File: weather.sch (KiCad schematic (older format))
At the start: 24 parts, among them J1 Tag-Connect, U1 nRF52810-QCxx, U2 HDC2080, Y1 32MHz, Y2 32kHz

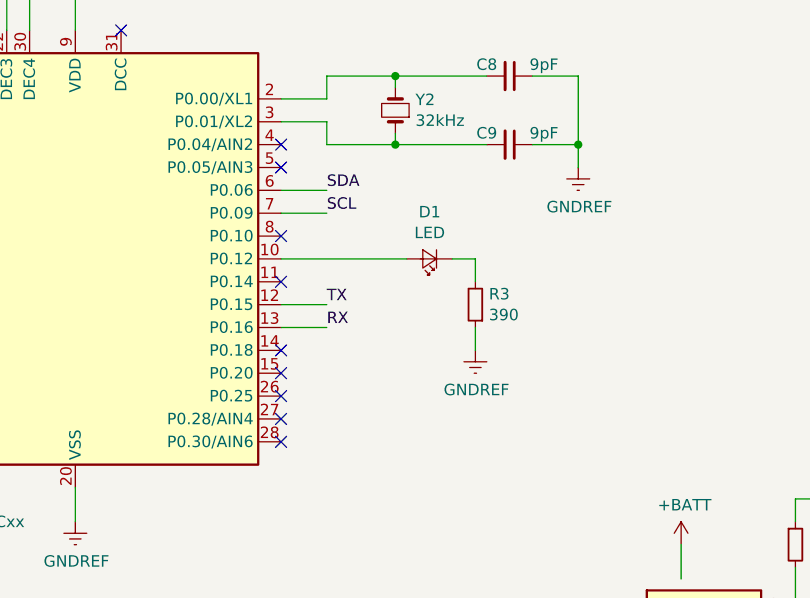
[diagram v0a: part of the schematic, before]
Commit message: Move LED to analog pin
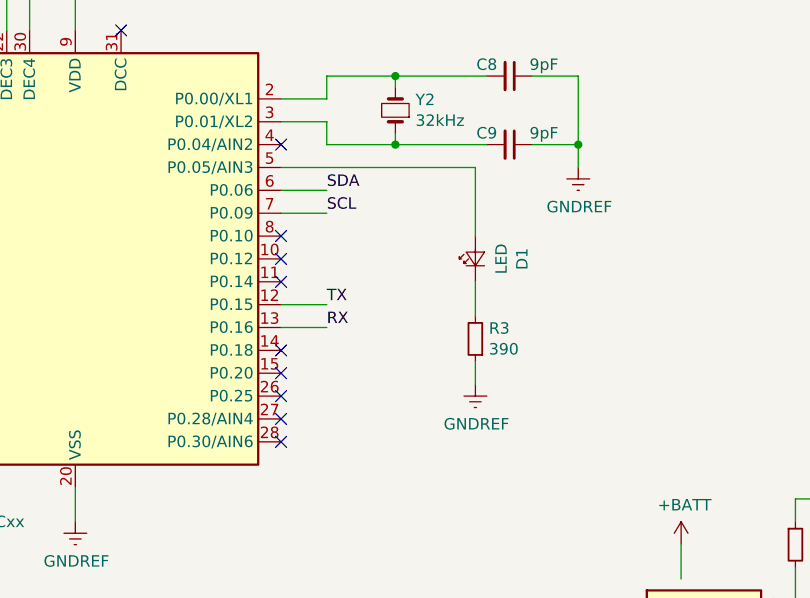
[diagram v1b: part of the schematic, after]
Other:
- moved on the sheet: D1, R3
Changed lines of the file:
@@
 NoConn ~ 4050 4250
 NoConn ~ 4050 3950
-NoConn ~ 4050 3450
+NoConn ~ 4050 3850
 NoConn ~ 4050 3350
 $Comp
@@
 L Device:LED_Small D1
 U 1 1 5B965F3F
-P 4700 3850
-F 0 "D1" H 4700 3645 50  0000 C CNN
-F 1 "LED" H 4700 3736 50  0000 C CNN
-F 2 "LED_SMD:LED_0603_1608Metric" V 4700 3850 50  0001 C CNN
-F 3 "~" V 4700 3850 50  0001 C CNN
-	1    4700 3850
-	-1   0    0    1
+P 4900 3850
+F 0 "D1" H 4900 3645 50  0000 C CNN
+F 1 "LED" H 4900 3736 50  0000 C CNN
+F 2 "LED_SMD:LED_0603_1608Metric" V 4900 3850 50  0001 C CNN
+F 3 "~" V 4900 3850 50  0001 C CNN
+	1    4900 3850
+	0    -1   -1   0
 $EndComp
 $Comp
 L Device:R_Small R3
 U 1 1 5B966096
-P 4900 4050
-F 0 "R3" H 4841 4004 50  0000 R CNN
-F 1 "390" H 4841 4095 50  0000 R CNN
-F 2 "Resistor_SMD:R_0603_1608Metric" H 4900 4050 50  0001 C CNN
-F 3 "~" H 4900 4050 50  0001 C CNN
-	1    4900 4050
+P 4900 4200
+F 0 "R3" H 4841 4154 50  0000 R CNN
+F 1 "390" H 4841 4245 50  0000 R CNN
+F 2 "Resistor_SMD:R_0603_1608Metric" H 4900 4200 50  0001 C CNN
+F 3 "~" H 4900 4200 50  0001 C CNN
+	1    4900 4200
 	-1   0    0    1
 $EndComp
@@
 L power:GNDREF #PWR0112
 U 1 1 5B9661A7
-P 4900 4250
-F 0 "#PWR0112" H 4900 4000 50  0001 C CNN
-F 1 "GNDREF" H 4905 4077 50  0000 C CNN
-F 2 "" H 4900 4250 50  0001 C CNN
-F 3 "" H 4900 4250 50  0001 C CNN
-	1    4900 4250
-	1    0    0    -1
-$EndComp
-Wire Wire Line
-	4900 4150 4900 4250
-Wire Wire Line
-	4900 3950 4900 3850
-Wire Wire Line
-	4900 3850 4800 3850
-Wire Wire Line
-	4600 3850 4050 3850
+P 4900 4400
+F 0 "#PWR0112" H 4900 4150 50  0001 C CNN
+F 1 "GNDREF" H 4905 4227 50  0000 C CNN
+F 2 "" H 4900 4400 50  0001 C CNN
+F 3 "" H 4900 4400 50  0001 C CNN
+	1    4900 4400
+	1    0    0    -1
+$EndComp
+Wire Wire Line
+	4900 4300 4900 4400
 NoConn ~ 4050 3750
 $Comp
@@
 Wire Wire Line
 	8400 4600 8400 4500
+Wire Wire Line
+	4900 3450 4900 3750
+Wire Wire Line
+	4050 3450 4900 3450
+Wire Wire Line
+	4900 3950 4900 4100
 $EndSCHEMATC

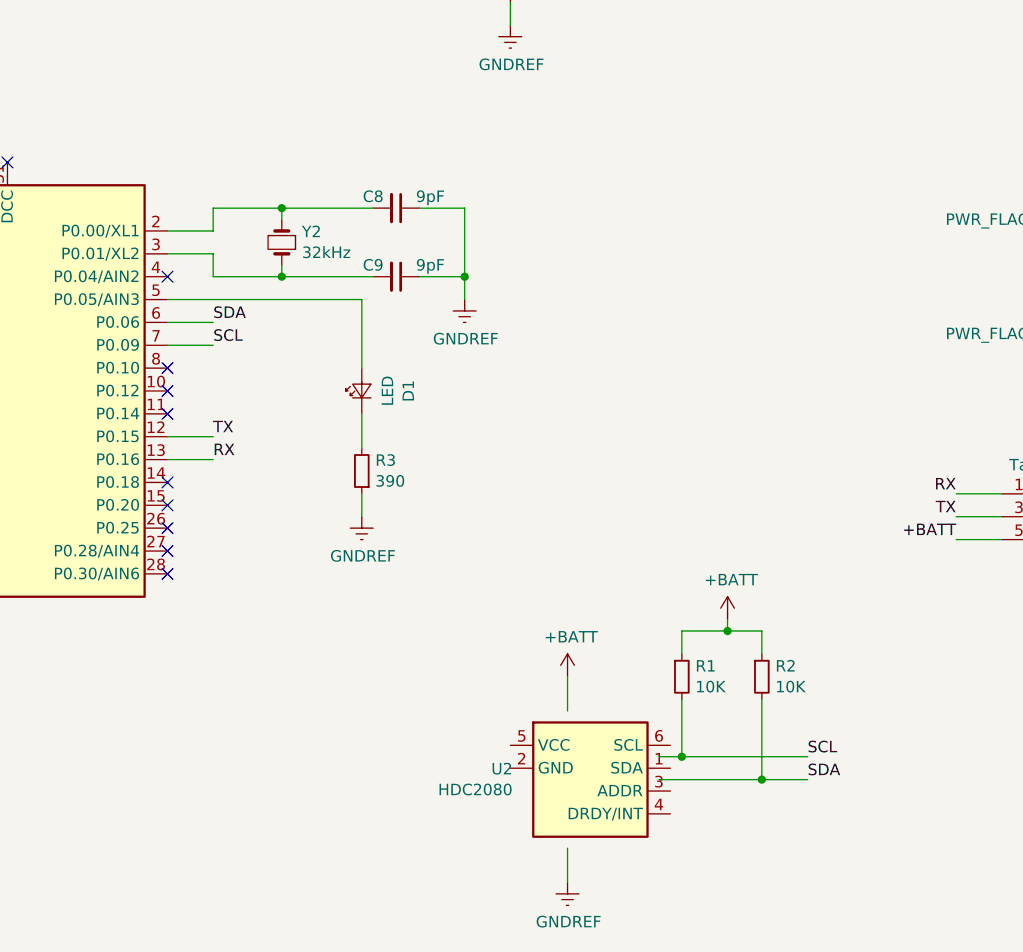
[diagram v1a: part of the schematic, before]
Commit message: HDC2080 DRDY / INT pin, and move LED pin
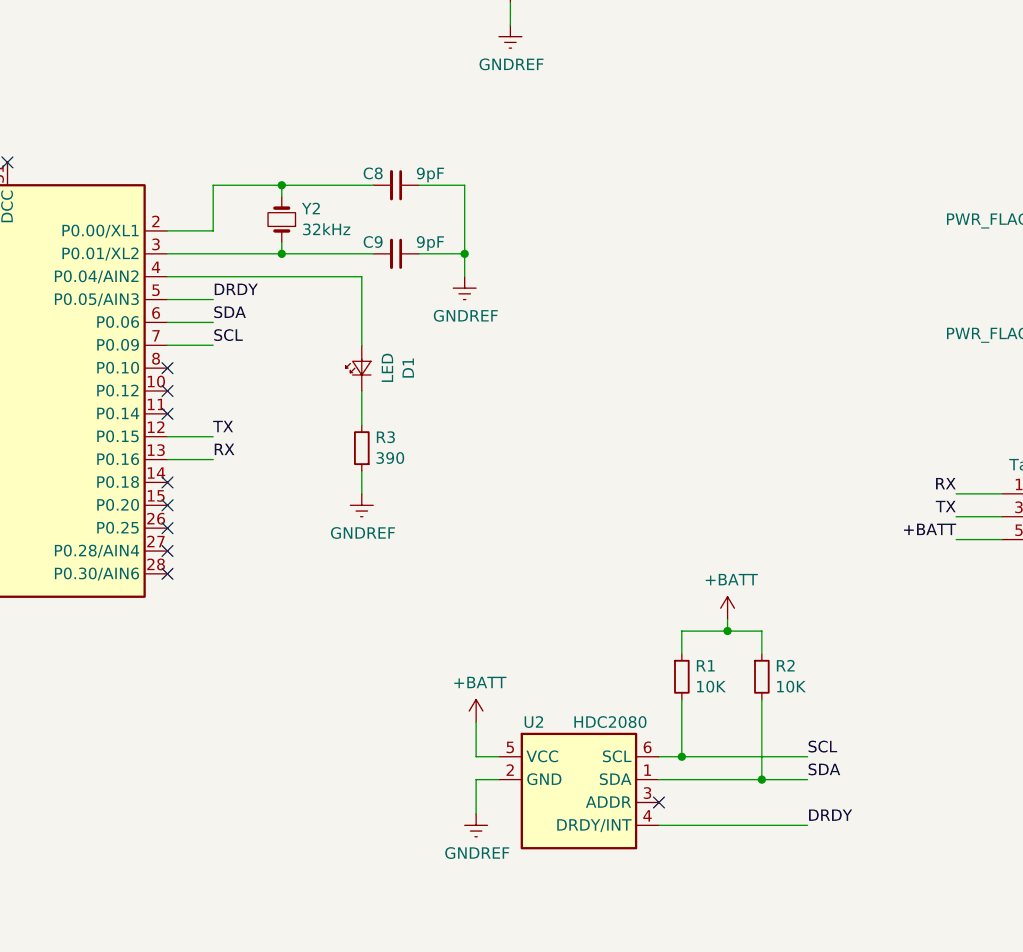
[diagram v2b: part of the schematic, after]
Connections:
- net labels added: DRDY
- wire segments 98 -> 100
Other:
- moved on the sheet: C8, C9, D1, R3, U2, Y2
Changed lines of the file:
@@
 L power:GNDREF #PWR0104
 U 1 1 5B7F3B6B
-P 5800 6000
-F 0 "#PWR0104" H 5800 5750 50  0001 C CNN
-F 1 "GNDREF" H 5805 5827 50  0000 C CNN
-F 2 "" H 5800 6000 50  0001 C CNN
-F 3 "" H 5800 6000 50  0001 C CNN
-	1    5800 6000
-	1    0    0    -1
-$EndComp
-Wire Wire Line
-	5800 5850 5800 6000
+P 5400 5700
+F 0 "#PWR0104" H 5400 5450 50  0001 C CNN
+F 1 "GNDREF" H 5405 5527 50  0000 C CNN
+F 2 "" H 5400 5700 50  0001 C CNN
+F 3 "" H 5400 5700 50  0001 C CNN
+	1    5400 5700
+	1    0    0    -1
+$EndComp
+Wire Wire Line
+	5400 5550 5400 5700
 $Comp
 L power:GNDREF #PWR0105
@@
 L power:+BATT #PWR0107
 U 1 1 5B7FB9F7
-P 5800 5100
-F 0 "#PWR0107" H 5800 4950 50  0001 C CNN
-F 1 "+BATT" H 5815 5273 50  0000 C CNN
-F 2 "" H 5800 5100 50  0001 C CNN
-F 3 "" H 5800 5100 50  0001 C CNN
-	1    5800 5100
+P 5400 5300
+F 0 "#PWR0107" H 5400 5150 50  0001 C CNN
+F 1 "+BATT" H 5415 5473 50  0000 C CNN
+F 2 "" H 5400 5300 50  0001 C CNN
+F 3 "" H 5400 5300 50  0001 C CNN
+	1    5400 5300
 	1    0    0    -1
 $EndComp
@@
 Connection ~ 3150 1800
 Wire Wire Line
-	5800 5100 5800 5250
+	5400 5300 5400 5450
 NoConn ~ 4050 4650
 NoConn ~ 4050 4550
@@
 NoConn ~ 4050 3950
 NoConn ~ 4050 3850
-NoConn ~ 4050 3350
 $Comp
 L Device:Battery_Cell BT1
@@
 L Anders_ICs:HDC2080 U2
 U 1 1 5B8027FD
-P 5900 5550
-F 0 "U2" H 5560 5596 50  0000 R CNN
-F 1 "HDC2080" H 5560 5505 50  0000 R CNN
-F 2 "Package_SON:Texas_PWSON-N6" H 5850 5300 50  0001 L CNN
-F 3 "http://www.ti.com/lit/ds/symlink/hdc2080.pdf" H 5500 5800 50  0001 C CNN
-	1    5900 5550
+P 5850 5600
+F 0 "U2" H 5700 5900 50  0000 R CNN
+F 1 "HDC2080" H 6150 5900 50  0000 R CNN
+F 2 "Package_SON:Texas_PWSON-N6" H 5800 5350 50  0001 L CNN
+F 3 "http://www.ti.com/lit/ds/symlink/hdc1080.pdf" H 5450 5850 50  0001 C CNN
+	1    5850 5600
 	1    0    0    -1
 $EndComp
@@
 L Device:Crystal_Small Y2
 U 1 1 5B840CE7
-P 4550 3200
-F 0 "Y2" V 4596 3112 50  0000 R CNN
-F 1 "32kHz" V 4505 3112 50  0000 R CNN
-F 2 "Crystal:Crystal_SMD_3215-2Pin_3.2x1.5mm" H 4550 3200 50  0001 C CNN
-F 3 "https://www.mouser.se/datasheet/2/741/LFXTAL009678Bulk-940165.pdf" H 4550 3200 50  0001 C CNN
-	1    4550 3200
+P 4550 3100
+F 0 "Y2" V 4596 3012 50  0000 R CNN
+F 1 "32kHz" V 4505 3012 50  0000 R CNN
+F 2 "Crystal:Crystal_SMD_3215-2Pin_3.2x1.5mm" H 4550 3100 50  0001 C CNN
+F 3 "https://www.mouser.se/datasheet/2/741/LFXTAL009678Bulk-940165.pdf" H 4550 3100 50  0001 C CNN
+	1    4550 3100
 	0    -1   -1   0
 $EndComp
@@
 L Device:C_Small C8
 U 1 1 5B840F1B
-P 5050 3050
-F 0 "C8" V 5000 2950 50  0000 C CNN
-F 1 "9pF" V 5000 3200 50  0000 C CNN
-F 2 "Capacitor_SMD:C_0603_1608Metric" H 5050 3050 50  0001 C CNN
-F 3 "~" H 5050 3050 50  0001 C CNN
-	1    5050 3050
+P 5050 2950
+F 0 "C8" V 5000 2850 50  0000 C CNN
+F 1 "9pF" V 5000 3100 50  0000 C CNN
+F 2 "Capacitor_SMD:C_0603_1608Metric" H 5050 2950 50  0001 C CNN
+F 3 "~" H 5050 2950 50  0001 C CNN
+	1    5050 2950
 	0    1    1    0
 $EndComp
@@
 L Device:C_Small C9
 U 1 1 5B8410C3
-P 5050 3350
-F 0 "C9" V 5000 3250 50  0000 C CNN
-F 1 "9pF" V 5000 3500 50  0000 C CNN
-F 2 "Capacitor_SMD:C_0603_1608Metric" H 5050 3350 50  0001 C CNN
-F 3 "~" H 5050 3350 50  0001 C CNN
-	1    5050 3350
+P 5050 3250
+F 0 "C9" V 5000 3150 50  0000 C CNN
+F 1 "9pF" V 5000 3400 50  0000 C CNN
+F 2 "Capacitor_SMD:C_0603_1608Metric" H 5050 3250 50  0001 C CNN
+F 3 "~" H 5050 3250 50  0001 C CNN
+	1    5050 3250
 	0    1    1    0
 $EndComp
@@
 	4050 3150 4250 3150
 Wire Wire Line
-	4250 3150 4250 3050
-Wire Wire Line
-	4250 3050 4550 3050
-Wire Wire Line
-	4050 3250 4250 3250
-Wire Wire Line
-	4250 3250 4250 3350
-Wire Wire Line
-	4250 3350 4550 3350
-Wire Wire Line
-	4550 3300 4550 3350
-Connection ~ 4550 3350
-Wire Wire Line
-	4550 3350 4950 3350
-Wire Wire Line
-	4550 3100 4550 3050
-Connection ~ 4550 3050
-Wire Wire Line
-	4550 3050 4950 3050
+	4250 2950 4550 2950
+Wire Wire Line
+	4550 3200 4550 3250
+Connection ~ 4550 3250
+Wire Wire Line
+	4550 3250 4950 3250
+Wire Wire Line
+	4550 3000 4550 2950
+Connection ~ 4550 2950
+Wire Wire Line
+	4550 2950 4950 2950
 $Comp
 L power:GNDREF #PWR0111
 U 1 1 5B8474FE
-P 5350 3450
-F 0 "#PWR0111" H 5350 3200 50  0001 C CNN
-F 1 "GNDREF" H 5355 3277 50  0000 C CNN
-F 2 "" H 5350 3450 50  0001 C CNN
-F 3 "" H 5350 3450 50  0001 C CNN
-	1    5350 3450
-	1    0    0    -1
-$EndComp
-Wire Wire Line
-	5150 3050 5350 3050
-Wire Wire Line
-	5350 3050 5350 3350
-Wire Wire Line
-	5150 3350 5350 3350
-Connection ~ 5350 3350
-Wire Wire Line
-	5350 3350 5350 3450
+P 5350 3350
+F 0 "#PWR0111" H 5350 3100 50  0001 C CNN
+F 1 "GNDREF" H 5355 3177 50  0000 C CNN
+F 2 "" H 5350 3350 50  0001 C CNN
+F 3 "" H 5350 3350 50  0001 C CNN
+	1    5350 3350
+	1    0    0    -1
+$EndComp
+Wire Wire Line
+	5150 2950 5350 2950
+Wire Wire Line
+	5350 2950 5350 3250
+Wire Wire Line
+	5150 3250 5350 3250
+Connection ~ 5350 3250
+Wire Wire Line
+	5350 3250 5350 3350
 $Comp
 L Device:C_Small C11
@@
 L Device:LED_Small D1
 U 1 1 5B965F3F
-P 4900 3850
-F 0 "D1" H 4900 3645 50  0000 C CNN
-F 1 "LED" H 4900 3736 50  0000 C CNN
-F 2 "LED_SMD:LED_0603_1608Metric" V 4900 3850 50  0001 C CNN
-F 3 "~" V 4900 3850 50  0001 C CNN
-	1    4900 3850
+P 4900 3750
+F 0 "D1" H 4900 3545 50  0000 C CNN
+F 1 "LED" H 4900 3636 50  0000 C CNN
+F 2 "LED_SMD:LED_0603_1608Metric" V 4900 3750 50  0001 C CNN
+F 3 "~" V 4900 3750 50  0001 C CNN
+	1    4900 3750
 	0    -1   -1   0
 $EndComp
@@
 L Device:R_Small R3
 U 1 1 5B966096
-P 4900 4200
-F 0 "R3" H 4841 4154 50  0000 R CNN
-F 1 "390" H 4841 4245 50  0000 R CNN
-F 2 "Resistor_SMD:R_0603_1608Metric" H 4900 4200 50  0001 C CNN
-F 3 "~" H 4900 4200 50  0001 C CNN
-	1    4900 4200
+P 4900 4100
+F 0 "R3" H 4841 4054 50  0000 R CNN
+F 1 "390" H 4841 4145 50  0000 R CNN
+F 2 "Resistor_SMD:R_0603_1608Metric" H 4900 4100 50  0001 C CNN
+F 3 "~" H 4900 4100 50  0001 C CNN
+	1    4900 4100
 	-1   0    0    1
 $EndComp
@@
 L power:GNDREF #PWR0112
 U 1 1 5B9661A7
-P 4900 4400
-F 0 "#PWR0112" H 4900 4150 50  0001 C CNN
-F 1 "GNDREF" H 4905 4227 50  0000 C CNN
-F 2 "" H 4900 4400 50  0001 C CNN
-F 3 "" H 4900 4400 50  0001 C CNN
-	1    4900 4400
-	1    0    0    -1
-$EndComp
-Wire Wire Line
-	4900 4300 4900 4400
+P 4900 4300
+F 0 "#PWR0112" H 4900 4050 50  0001 C CNN
+F 1 "GNDREF" H 4905 4127 50  0000 C CNN
+F 2 "" H 4900 4300 50  0001 C CNN
+F 3 "" H 4900 4300 50  0001 C CNN
+	1    4900 4300
+	1    0    0    -1
+$EndComp
+Wire Wire Line
+	4900 4200 4900 4300
 NoConn ~ 4050 3750
 $Comp
@@
 	8400 4600 8400 4500
 Wire Wire Line
-	4900 3450 4900 3750
-Wire Wire Line
-	4050 3450 4900 3450
-Wire Wire Line
-	4900 3950 4900 4100
+	4900 3350 4900 3650
+Wire Wire Line
+	4050 3350 4900 3350
+Wire Wire Line
+	4900 3850 4900 4000
+Wire Wire Line
+	5400 5450 5500 5450
+Wire Wire Line
+	5400 5550 5500 5550
+NoConn ~ 6200 5650
+Wire Wire Line
+	4050 3250 4550 3250
+Wire Wire Line
+	4250 2950 4250 3150
+Text Label 4250 3450 0    50   ~ 0
+DRDY
+Wire Wire Line
+	4250 3450 4050 3450
+Text Label 6850 5750 0    50   ~ 0
+DRDY
+Wire Wire Line
+	6850 5750 6200 5750
 $EndSCHEMATC

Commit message: KiCad upgrade
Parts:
- Y1: symbol Device:Crystal_GND24_Small -> weather-rescue:Crystal_GND24_Small-Device
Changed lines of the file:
@@
 EESchema Schematic File Version 4
 LIBS:weather-cache
-EELAYER 26 0
+EELAYER 29 0
 EELAYER END
 $Descr A4 11693 8268
@@
 Sheet 1 1
 Title ""
-Date "2018-09-07"
-Rev "1.0"
+Date "2019-03-29"
+Rev "1.1"
 Comp ""
 Comment1 ""
@@
 $EndComp
 $Comp
-L Device:Crystal_GND24_Small Y1
+L weather-rescue:Crystal_GND24_Small-Device Y1
 U 1 1 5B7EBD1C
 P 1650 3850
@@
 	6650 5550 6850 5550
 $Comp
-L Anders_ICs:HDC2080 U2
-U 1 1 5B8027FD
-P 5850 5600
-F 0 "U2" H 5700 5900 50  0000 R CNN
-F 1 "HDC2080" H 6150 5900 50  0000 R CNN
-F 2 "Package_SON:Texas_PWSON-N6" H 5800 5350 50  0001 L CNN
-F 3 "http://www.ti.com/lit/ds/symlink/hdc1080.pdf" H 5450 5850 50  0001 C CNN
-	1    5850 5600
-	1    0    0    -1
-$EndComp
-$Comp
 L Device:Crystal_Small Y2
 U 1 1 5B840CE7
@@
 Wire Wire Line
 	6850 5750 6200 5750
+$Comp
+L Anders_ICs:HDC2080 U2
+U 1 1 5BBE39A8
+P 5850 5600
+F 0 "U2" H 5850 6017 50  0000 C CNN
+F 1 "HDC2080" H 5850 5926 50  0000 C CNN
+F 2 "Package_SON:Texas_PWSON-N6" H 5850 5300 50  0001 L CNN
+F 3 "http://www.ti.com/lit/ds/symlink/hdc2080.pdf" H 5500 5900 50  0001 C CNN
+	1    5850 5600
+	1    0    0    -1
+$EndComp
 $EndSCHEMATC
